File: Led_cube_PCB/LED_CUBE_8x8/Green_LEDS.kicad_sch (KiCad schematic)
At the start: 2 parts, among them IC26 74AHC138PW,118

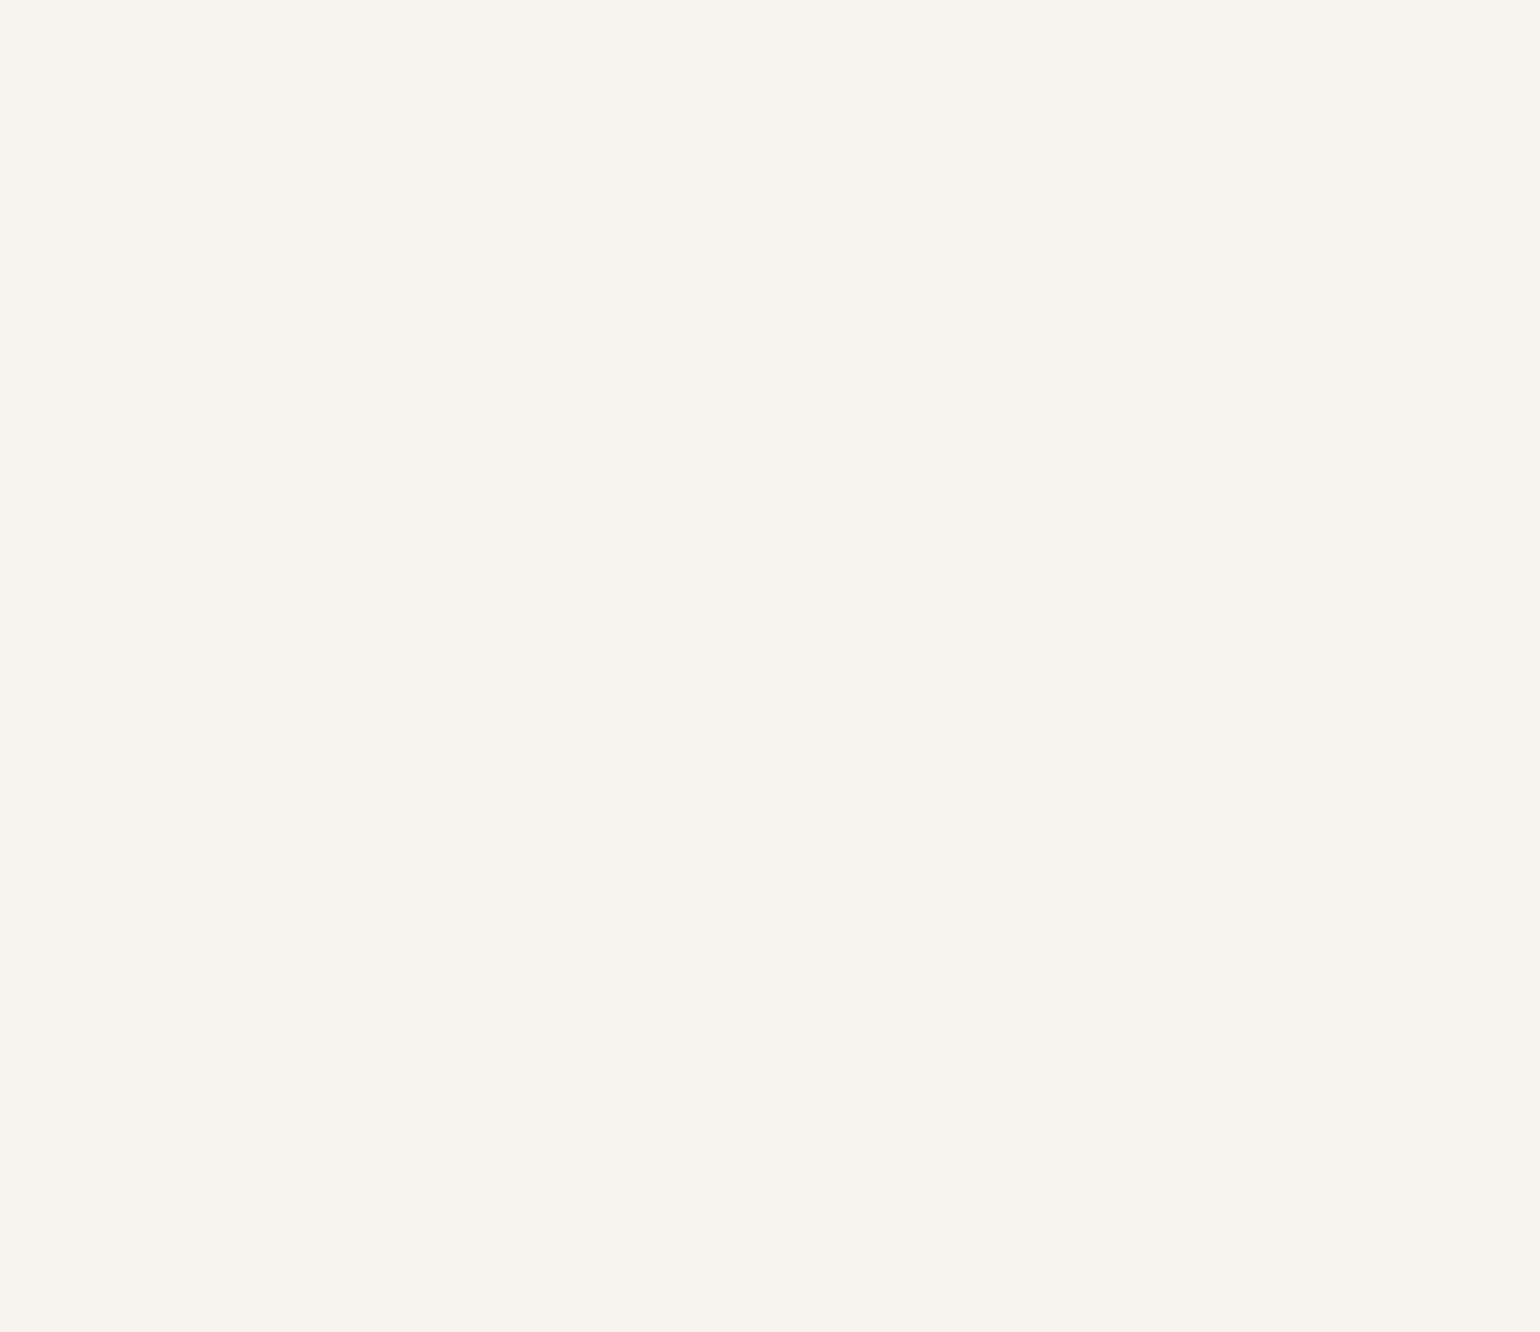
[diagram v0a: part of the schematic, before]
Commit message: Finished the schematic for the red green and blue color multiplexing.
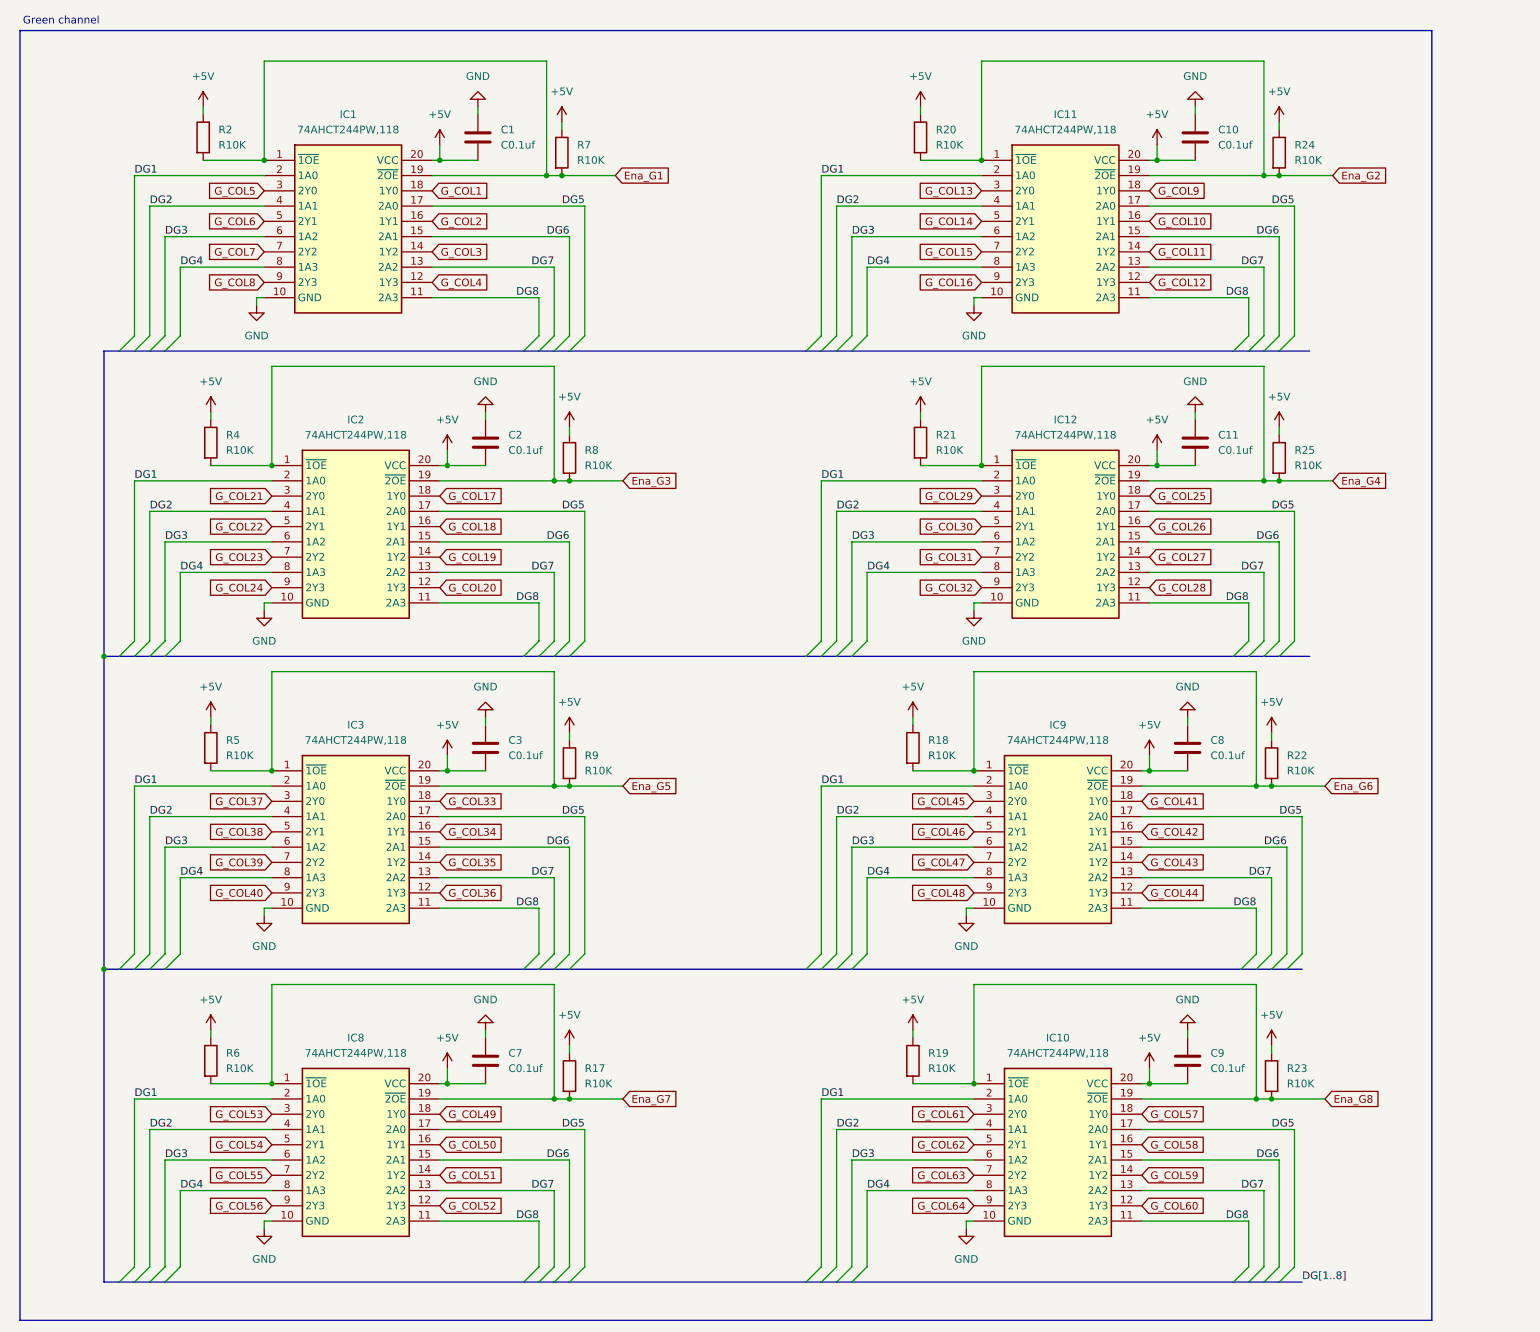
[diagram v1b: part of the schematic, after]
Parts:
- added C1, C10, C11, C2, C3, C7, C8, C9: C0.1uf, symbol Device:C
- added IC1, IC10, IC11, IC12, IC2, IC3, IC8, IC9: 74AHCT244PW,118, SOP65P640X110-20N, symbol SamacSys_Parts:74AHCT244PW,118
- added R17, R18, R19, R2, R20, R21, R22, R23, R24, R25, R4, R5, R6, R7, R8, R9: R10K, symbol Device:R
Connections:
- net +5V: now also C1.2, C10.2, C11.2, C2.2, C3.2, C7.2, C8.2, C9.2, IC1.20 (VCC), IC10.20 (VCC), IC11.20 (VCC), IC12.20 (VCC), IC2.20 (VCC), IC3.20 (VCC), IC8.20 (VCC), IC9.20 (VCC), R17.1, R18.1, R19.1, R2.1, R20.1, R21.1, R22.1, R23.1, R24.1, R25.1, R4.1, R5.1, R6.1, R7.1, R8.1, R9.1
- net Ena_G1: now also IC1.1 (~{1OE}), IC1.19 (~{2OE}), R2.2, R7.2
- net Ena_G2: now also IC11.1 (~{1OE}), IC11.19 (~{2OE}), R20.2, R24.2
- net Ena_G3: now also IC2.1 (~{1OE}), IC2.19 (~{2OE}), R4.2, R8.2
- net Ena_G4: now also IC12.1 (~{1OE}), IC12.19 (~{2OE}), R21.2, R25.2
- net Ena_G5: now also IC3.1 (~{1OE}), IC3.19 (~{2OE}), R5.2, R9.2
- net Ena_G6: now also IC9.1 (~{1OE}), IC9.19 (~{2OE}), R18.2, R22.2
- net Ena_G7: now also IC8.1 (~{1OE}), IC8.19 (~{2OE}), R17.2, R6.2
- net Ena_G8: now also IC10.1 (~{1OE}), IC10.19 (~{2OE}), R19.2, R23.2
- net GND: now also C1.1, C10.1, C11.1, C2.1, C3.1, C7.1, C8.1, C9.1, IC1.10 (GND), IC10.10 (GND), IC11.10 (GND), IC12.10 (GND), IC2.10 (GND), IC3.10 (GND), IC8.10 (GND), IC9.10 (GND)
- new net DG1: IC1.2 (1A0), IC10.2 (1A0), IC11.2 (1A0), IC12.2 (1A0), IC2.2 (1A0), IC3.2 (1A0), IC8.2 (1A0), IC9.2 (1A0)
- new net DG2: IC1.4 (1A1), IC10.4 (1A1), IC11.4 (1A1), IC12.4 (1A1), IC2.4 (1A1), IC3.4 (1A1), IC8.4 (1A1), IC9.4 (1A1)
- new net DG3: IC1.6 (1A2), IC10.6 (1A2), IC11.6 (1A2), IC12.6 (1A2), IC2.6 (1A2), IC3.6 (1A2), IC8.6 (1A2), IC9.6 (1A2)
- new net DG4: IC1.8 (1A3), IC10.8 (1A3), IC11.8 (1A3), IC12.8 (1A3), IC2.8 (1A3), IC3.8 (1A3), IC8.8 (1A3), IC9.8 (1A3)
- new net DG5: IC1.17 (2A0), IC10.17 (2A0), IC11.17 (2A0), IC12.17 (2A0), IC2.17 (2A0), IC3.17 (2A0), IC8.17 (2A0), IC9.17 (2A0)
- new net DG6: IC1.15 (2A1), IC10.15 (2A1), IC11.15 (2A1), IC12.15 (2A1), IC2.15 (2A1), IC3.15 (2A1), IC8.15 (2A1), IC9.15 (2A1)
- new net DG7: IC1.13 (2A2), IC10.13 (2A2), IC11.13 (2A2), IC12.13 (2A2), IC2.13 (2A2), IC3.13 (2A2), IC8.13 (2A2), IC9.13 (2A2)
- new net DG8: IC1.11 (2A3), IC10.11 (2A3), IC11.11 (2A3), IC12.11 (2A3), IC2.11 (2A3), IC3.11 (2A3), IC8.11 (2A3), IC9.11 (2A3)
- new net G_COL1: IC1.18 (1Y0)
- new net G_COL10: IC11.16 (1Y1)
- new net G_COL11: IC11.14 (1Y2)
- new net G_COL12: IC11.12 (1Y3)
- new net G_COL13: IC11.3 (2Y0)
- new net G_COL14: IC11.5 (2Y1)
- new net G_COL15: IC11.7 (2Y2)
- new net G_COL16: IC11.9 (2Y3)
- new net G_COL17: IC2.18 (1Y0)
- new net G_COL18: IC2.16 (1Y1)
- new net G_COL19: IC2.14 (1Y2)
- new net G_COL2: IC1.16 (1Y1)
- new net G_COL20: IC2.12 (1Y3)
- new net G_COL21: IC2.3 (2Y0)
- new net G_COL22: IC2.5 (2Y1)
- new net G_COL23: IC2.7 (2Y2)
- new net G_COL24: IC2.9 (2Y3)
- new net G_COL25: IC12.18 (1Y0)
- new net G_COL26: IC12.16 (1Y1)
- new net G_COL27: IC12.14 (1Y2)
- new net G_COL28: IC12.12 (1Y3)
- new net G_COL29: IC12.3 (2Y0)
- new net G_COL3: IC1.14 (1Y2)
- new net G_COL30: IC12.5 (2Y1)
- new net G_COL31: IC12.7 (2Y2)
- new net G_COL32: IC12.9 (2Y3)
- new net G_COL33: IC3.18 (1Y0)
- new net G_COL34: IC3.16 (1Y1)
- new net G_COL35: IC3.14 (1Y2)
- new net G_COL36: IC3.12 (1Y3)
- new net G_COL37: IC3.3 (2Y0)
- new net G_COL38: IC3.5 (2Y1)
- new net G_COL39: IC3.7 (2Y2)
- new net G_COL4: IC1.12 (1Y3)
- new net G_COL40: IC3.9 (2Y3)
- new net G_COL41: IC9.18 (1Y0)
- new net G_COL42: IC9.16 (1Y1)
- new net G_COL43: IC9.14 (1Y2)
- new net G_COL44: IC9.12 (1Y3)
- new net G_COL45: IC9.3 (2Y0)
- new net G_COL46: IC9.5 (2Y1)
- new net G_COL47: IC9.7 (2Y2)
- new net G_COL48: IC9.9 (2Y3)
- new net G_COL49: IC8.18 (1Y0)
- new net G_COL5: IC1.3 (2Y0)
- new net G_COL50: IC8.16 (1Y1)
- new net G_COL51: IC8.14 (1Y2)
- new net G_COL52: IC8.12 (1Y3)
- new net G_COL53: IC8.3 (2Y0)
- new net G_COL54: IC8.5 (2Y1)
- new net G_COL55: IC8.7 (2Y2)
- new net G_COL56: IC8.9 (2Y3)
- new net G_COL57: IC10.18 (1Y0)
- new net G_COL58: IC10.16 (1Y1)
- new net G_COL59: IC10.14 (1Y2)
- new net G_COL6: IC1.5 (2Y1)
- new net G_COL60: IC10.12 (1Y3)
- new net G_COL61: IC10.3 (2Y0)
- new net G_COL62: IC10.5 (2Y1)
- new net G_COL63: IC10.7 (2Y2)
- new net G_COL64: IC10.9 (2Y3)
- new net G_COL7: IC1.7 (2Y2)
- new net G_COL8: IC1.9 (2Y3)
- new net G_COL9: IC11.18 (1Y0)
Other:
- note added: "Green channel"
- company: (none) -> Áuthor: Lars Molenschot
- title: Green LED's -> 8x8_Led_Cube
